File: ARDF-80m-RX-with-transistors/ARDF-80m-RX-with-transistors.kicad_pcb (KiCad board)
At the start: 2 copper layers, 44.5 x 26 mm, 45 parts, among them J1 JACK, Q1 BC847, Q2 BC847, Q3 BC847, Q4 BC847, Q5 BC847, U1 LM358, Y1 3.5795MHz

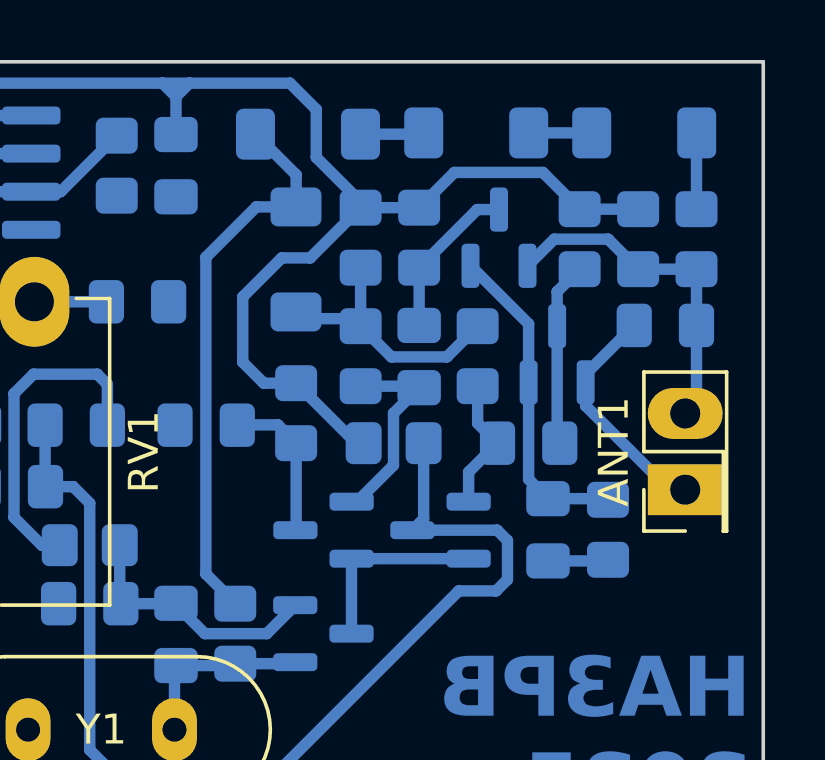
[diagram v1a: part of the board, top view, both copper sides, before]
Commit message: Update diodes packaging
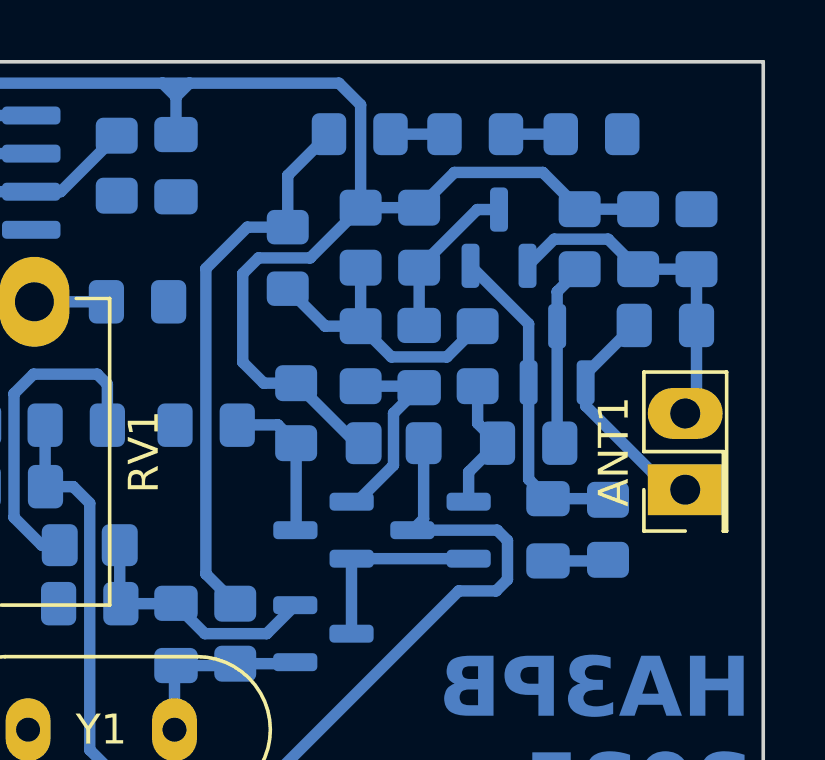
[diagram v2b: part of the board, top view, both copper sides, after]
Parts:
- D1, D2, D3, D5: footprint Diode_SMD:D_MiniMELF -> Diode_SMD:D_0805_2012Metric_Pad1.15x1.40mm_HandSolder
- moved D5 1.76 mm to (89.2, 79.8)
- moved D2 1.72 mm to (81.5, 79.8)
- moved D1 0.28 mm to (79.1, 84.0)
- moved D3 0.05 mm to (85.3, 79.8)
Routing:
- net GND: track 15.5 -> 12.9 mm
- net VCC: track 86.8 -> 88.2 mm
- net /BIAS: track 9.05 -> 9.65 mm

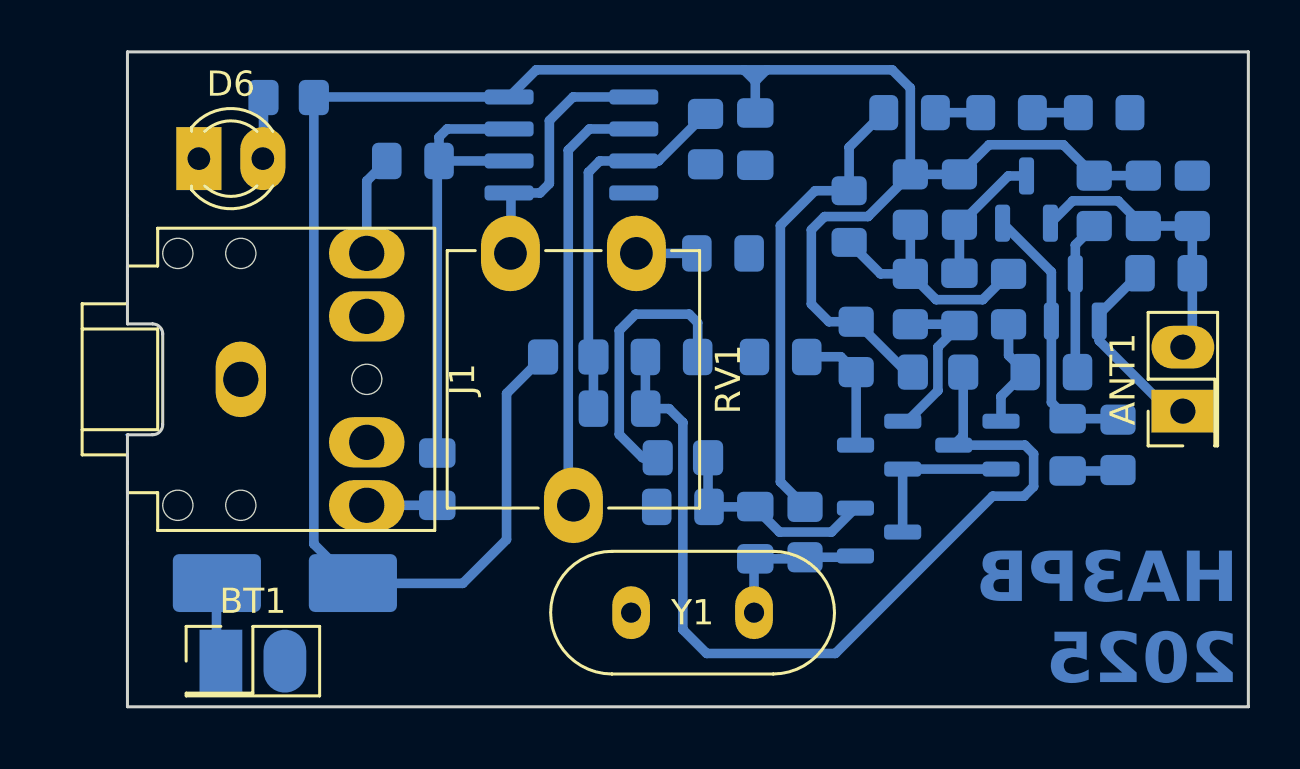
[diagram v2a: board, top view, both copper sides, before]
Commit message: Update jack connector footprint
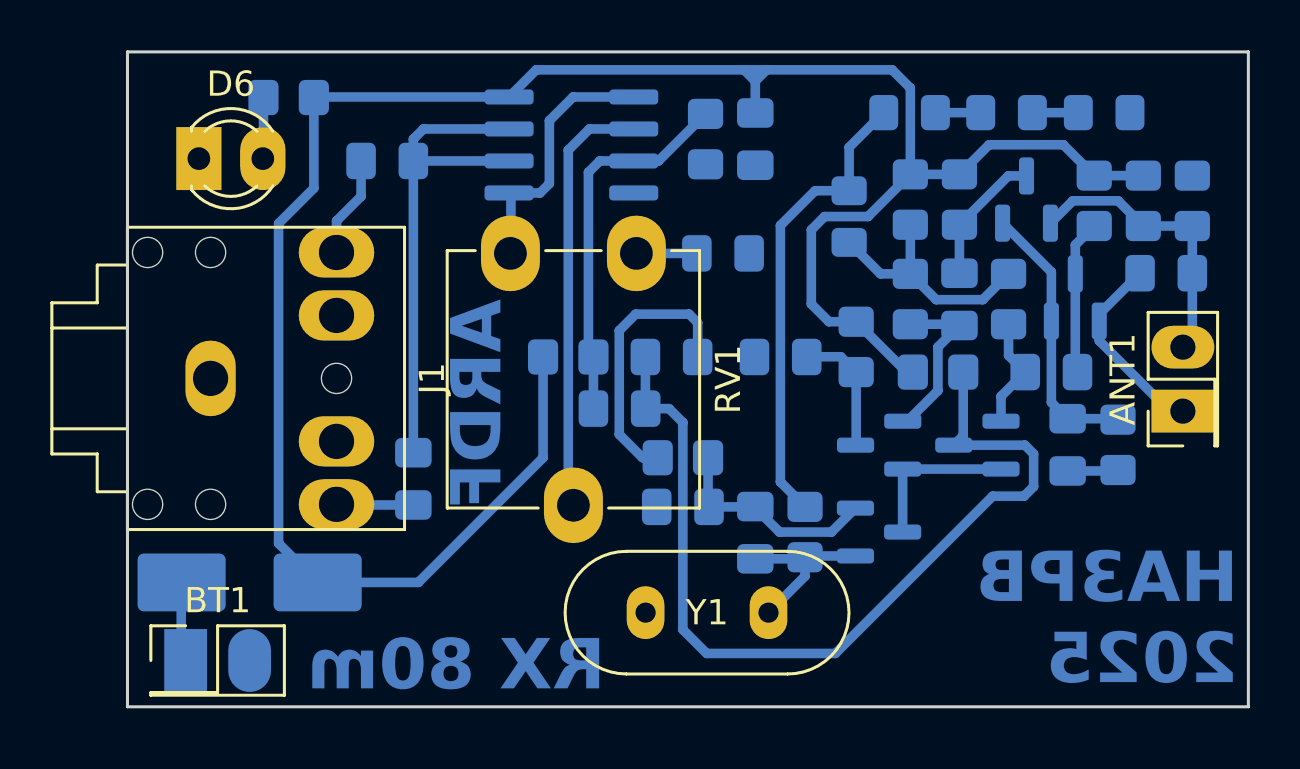
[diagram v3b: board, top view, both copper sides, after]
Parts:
- moved D4 1.40 mm to (55.3, 98.5)
- moved BT1 1.40 mm to (52.8, 101.6)
- moved J1 1.20 mm to (53.8, 90.4)
- moved C5 1.02 mm to (60.8, 81.8)
- moved C7 0.95 mm to (61.8, 94.4)
- moved Y1 0.58 mm to (71.0, 99.7)
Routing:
- net Net-(U1B--): track 18.3 -> 20.2 mm
- net VCC: track 88.2 -> 89.1 mm
- net Net-(Q5-B): track 6.21 -> 6.82 mm
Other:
- outline, holes or cut-outs redrawn
- board text added: "ARDF"
- board text added: "RX 80m"
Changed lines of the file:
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@@
 	(footprint "Crystal:Crystal_HC49-4H_Vertical"
 		(layer "F.Cu")
-		(at 70.445 99.7)
+		(at 71.02 99.7)
 		(descr "HC-49-4H, Crystal, http://5hertz.com/pdfs/04404_D.pdf")
 		(property "Reference" "Y1"
@@
 	(footprint "Connector_Audio:Jack_3.5mm_CUI_SJ1-3525N_Horizontal"
 		(layer "F.Cu")
-		(at 54.95 90.4375 -90)
+		(at 53.75 90.4 -90)
 		(descr "TRS 3.5mm, horizontal, through-hole, https://www.cuidevices.com/product/resource/pdf/sj1-352xn.pdf")
 		(tags "TRS audio jack stereo horizontal")
@@
 		)
 		(fp_line
-			(start -2.2 4.5)
-			(end -6.5 4.5)
-			(stroke
-				(width 0.12)
-				(type solid)
-			)
-			(layer "Edge.Cuts")
-		)
-		(fp_line
-			(start 2.2 4.5)
-			(end 6.5 4.5)
-			(stroke
-				(width 0.12)
-				(type solid)
-			)
-			(layer "Edge.Cuts")
-		)
-		(fp_line
-			(start -2.2 3.5)
-			(end -2.2 4.5)
-			(stroke
-				(width 0.12)
-				(type solid)
-			)
-			(layer "Edge.Cuts")
-		)
-		(fp_line
-			(start 2.2 3.5)
-			(end 2.2 4.5)
-			(stroke
-				(width 0.12)
-				(type solid)
-			)
-			(layer "Edge.Cuts")
-		)
-		(fp_line
-			(start 1.8 3.1)
-			(end -1.8 3.1)
-			(stroke
-				(width 0.12)
-				(type solid)
-			)
-			(layer "Edge.Cuts")
-		)
-		(fp_arc
-			(start -2.2 3.5)
-			(mid -2.082842 3.217158)
-			(end -1.8 3.1)
-			(stroke
-				(width 0.12)
-				(type solid)
-			)
-			(layer "Edge.Cuts")
-		)
-		(fp_arc
-			(start 1.8 3.1)
-			(mid 2.082843 3.217157)
-			(end 2.2 3.5)
+			(start 6.6376 3.3)
+			(end -6.6376 3.3)
 			(stroke
 				(width 0.12)
@@
 	(footprint "Connector_PinHeader_2.54mm:PinHeader_2x01_P2.54mm_Vertical"
 		(layer "F.Cu")
-		(at 54.16 101.625)
+		(at 52.76 101.6)
 		(descr "Through hole straight pin header, 2x01, 2.54mm pitch, double rows")
 		(tags "Through hole pin header THT 2x01 2.54mm double row")
@@
 	(footprint "Diode_SMD:D_SMB_Handsoldering"
 		(layer "B.Cu")
-		(at 56.7 98.525 180)
+		(at 55.3 98.5 180)
 		(descr "Diode SMB (DO-214AA) Handsoldering")
 		(tags "Diode SMB (DO-214AA) Handsoldering")
@@
 	(footprint "Capacitor_SMD:C_0805_2012Metric_Pad1.18x1.45mm_HandSolder"
 		(layer "B.Cu")
-		(at 62.75 94.4 90)
+		(at 61.8 94.3875 90)
 		(descr "Capacitor SMD 0805 (2012 Metric), square (rectangular) end terminal, IPC-7351 nominal with elongated pad for handsoldering. (Body size source: IPC-SM-782 page 76, https://www.pcb-3d.com/wordpress/wp-content/uploads/ipc-sm-782a_amendment_1_and_2.pdf, https://docs.google.com/spreadsheets/d/1BsfQQcO9C6DZCsRaXUlFlo91Tg2WpOkGARC1WS5S8t0/edit?usp=sharing), generated with kicad-footprint-generator")
 		(tags "capacitor handsolder")
@@
 	(footprint "Capacitor_SMD:C_0805_2012Metric_Pad1.18x1.45mm_HandSolder"
 		(layer "B.Cu")
-		(at 61.7825 81.7675 180)
+		(at 60.7625 81.7675 180)
 		(descr "Capacitor SMD 0805 (2012 Metric), square (rectangular) end terminal, IPC-7351 nominal with elongated pad for handsoldering. (Body size source: IPC-SM-782 page 76, https://www.pcb-3d.com/wordpress/wp-content/uploads/ipc-sm-782a_amendment_1_and_2.pdf, https://docs.google.com/spreadsheets/d/1BsfQQcO9C6DZCsRaXUlFlo91Tg2WpOkGARC1WS5S8t0/edit?usp=sharing), generated with kicad-footprint-generator")
 		(tags "capacitor handsolder")
@@
 	)
 	(gr_line
-		(start 50.45 96.9375)
+		(start 50.45 97.0376)
 		(end 50.45 103.4375)
 		(stroke
@@
 	)
 	(gr_line
-		(start 50.45 83.9375)
+		(start 50.45 83.7624)
 		(end 50.45 77.4375)
 		(stroke
@@
 		)
 	)
+	(gr_text "RX 80m"
+		(at 63.5 102.95 0)
+		(layer "B.Cu" knockout)
+		(effects
+			(font
+				(size 2 2)
+				(thickness 0.5)
+				(bold yes)
+			)
+			(justify bottom mirror)
+		)
+	)
+	(gr_text "ARDF"
+		(at 65.5 87.25 90)
+		(layer "B.Cu")
+		(effects
+			(font
+				(size 2 2)
+				(thickness 0.5)
+				(bold yes)
+			)
+			(justify left bottom mirror)
+		)
+	)
 	(segment
 		(start 89.03 88.905)
@@
 	)
 	(segment
-		(start 54.16 101.625)
-		(end 53.985 101.45)
+		(start 52.76 101.6)
+		(end 52.585 101.425)
 		(width 0.381)
 		(layer "B.Cu")
@@
 	)
 	(segment
-		(start 53.985 101.45)
-		(end 53.985 98.6975)
+		(start 52.585 101.425)
+		(end 52.585 98.6725)
 		(width 0.381)
 		(layer "B.Cu")
@@
 	)
 	(segment
-		(start 53.985 98.6975)
-		(end 53.825 98.5375)
+		(start 52.585 98.6725)
+		(end 52.425 98.5125)
 		(width 0.381)
 		(layer "B.Cu")
@@
 	)
 	(segment
-		(start 65.6 80.4975)
-		(end 63.14 80.4975)
+		(start 61.8 93.35)
+		(end 61.8 81.7675)
 		(width 0.381)
 		(layer "B.Cu")
@@
 	)
 	(segment
-		(start 62.82 80.8175)
-		(end 62.82 81.7675)
+		(start 65.6 81.7675)
+		(end 61.8 81.7675)
 		(width 0.381)
 		(layer "B.Cu")
@@
 	)
 	(segment
-		(start 62.82 81.7675)
-		(end 62.82 82.0675)
+		(start 62.2025 80.4975)
+		(end 61.8 80.9)
 		(width 0.381)
 		(layer "B.Cu")
@@
 	)
 	(segment
-		(start 62.75 82.1375)
-		(end 62.75 93.3625)
+		(start 61.8 80.9)
+		(end 61.8 81.7675)
 		(width 0.381)
 		(layer "B.Cu")
@@
 	)
 	(segment
-		(start 65.6 81.7675)
-		(end 62.82 81.7675)
+		(start 65.6 80.4975)
+		(end 62.2025 80.4975)
 		(width 0.381)
 		(layer "B.Cu")
@@
 	)
 	(segment
-		(start 62.82 82.0675)
-		(end 62.75 82.1375)
+		(start 58.75 85.4)
+		(end 58.75 84.15)
 		(width 0.381)
 		(layer "B.Cu")
-		(net 12)
+		(net 13)
 	)
 	(segment
-		(start 63.14 80.4975)
-		(end 62.82 80.8175)
+		(start 59.725 83.175)
+		(end 59.725 81.7675)
 		(width 0.381)
 		(layer "B.Cu")
-		(net 12)
+		(net 13)
 	)
 	(segment
-		(start 59.95 85.4375)
-		(end 59.95 82.5625)
+		(start 58.75 84.15)
+		(end 59.725 83.175)
 		(width 0.381)
 		(layer "B.Cu")
@@
 	)
 	(segment
-		(start 59.95 82.5625)
-		(end 60.745 81.7675)
+		(start 58.775 95.425)
+		(end 58.75 95.4)
 		(width 0.381)
 		(layer "B.Cu")
-		(net 13)
+		(net 14)
 	)
 	(segment
-		(start 62.75 95.4375)
-		(end 59.95 95.4375)
+		(start 61.8 95.425)
+		(end 58.775 95.425)
 		(width 0.381)
 		(layer "B.Cu")
@@
 	)
 	(segment
-		(start 79.3 97.5)
-		(end 79.35 97.45)
+		(start 77.35 98.25)
+		(end 75.9 99.7)
 		(width 0.381)
 		(layer "B.Cu")
@@
 	)
 	(segment
-		(start 75.325 99.7)
-		(end 75.325 97.5625)
+		(start 79.35 97.45)
+		(end 77.4 97.45)
 		(width 0.381)
 		(layer "B.Cu")
@@
 	)
 	(segment
-		(start 75.325 97.5625)
-		(end 77.2375 97.5625)
+		(start 77.2875 97.5625)
+		(end 77.35 97.5)
 		(width 0.381)
 		(layer "B.Cu")
@@
 	)
 	(segment
-		(start 77.3 97.5)
-		(end 79.3 97.5)
+		(start 75.375 97.5625)
+		(end 77.2875 97.5625)
 		(width 0.381)
 		(layer "B.Cu")
@@
 	)
 	(segment
-		(start 77.2375 97.5625)
-		(end 77.3 97.5)
+		(start 77.4 97.45)
+		(end 77.35 97.5)
+		(width 0.381)
+		(layer "B.Cu")
+		(net 17)
+	)
+	(segment
+		(start 77.35 97.5)
+		(end 77.35 98.25)
 		(width 0.381)
 		(layer "B.Cu")
@@
 	)
 	(segment
-		(start 57.85 96.975)
-		(end 59.4125 98.5375)
-		(width 0.381)
-		(layer "B.Cu")
-		(net 23)
-	)
-	(segment
-		(start 59.4125 98.5375)
-		(end 63.7625 98.5375)
-		(width 0.381)
-		(layer "B.Cu")
-		(net 23)
-	)
-	(segment
 		(start 81.63 90.15)
 		(end 81.38 90.15)
@@
 	)
 	(segment
-		(start 65.5 96.8)
-		(end 65.5 91)
+		(start 66.95 93.55)
+		(end 62 98.5)
 		(width 0.381)
 		(layer "B.Cu")
@@
 	)
 	(segment
+		(start 57.85 82.85)
+		(end 57.85 79.25)
+		(width 0.381)
+		(layer "B.Cu")
+		(net 23)
+	)
+	(segment
 		(start 83.48 82.3)
 		(end 84.655 81.125)
@@
 	)
 	(segment
+		(start 62 98.5)
+		(end 58 98.5)
+		(width 0.381)
+		(layer "B.Cu")
+		(net 23)
+	)
+	(segment
 		(start 74.925 78.15)
 		(end 66.6775 78.15)
@@
 	)
 	(segment
-		(start 63.7625 98.5375)
-		(end 65.5 96.8)
-		(width 0.381)
-		(layer "B.Cu")
-		(net 23)
-	)
-	(segment
 		(start 75.825 78.15)
 		(end 80.807072 78.15)
@@
 	)
 	(segment
-		(start 65.5 91)
-		(end 66.95 89.55)
+		(start 87.605 81.125)
+		(end 88.83 82.35)
 		(width 0.381)
 		(layer "B.Cu")
@@
 	)
 	(segment
-		(start 87.605 81.125)
-		(end 88.83 82.35)
+		(start 66.95 89.55)
+		(end 66.95 93.55)
 		(width 0.381)
 		(layer "B.Cu")
@@
 	)
 	(segment
+		(start 58 98.5)
+		(end 56.45 96.95)
+		(width 0.381)
+		(layer "B.Cu")
+		(net 23)
+	)
+	(segment
 		(start 80.807072 78.15)
 		(end 81.53 78.872928)
@@
 	)
 	(segment
+		(start 56.45 96.95)
+		(end 56.45 84.25)
+		(width 0.381)
+		(layer "B.Cu")
+		(net 23)
+	)
+	(segment
 		(start 77.6 87.45)
 		(end 78.3 88.15)
@@
 	)
 	(segment
-		(start 57.85 79.25)
-		(end 57.85 96.975)
+		(start 56.45 84.25)
+		(end 57.85 82.85)
 		(width 0.381)
 		(layer "B.Cu")
@@
 		(polygon
 			(pts
-				(xy 50.45 77.4375) (xy 50.45 88.2375) (xy 51.45 88.2375) (xy 51.732843 88.354658) (xy 51.85 88.6375)
-				(xy 51.85 92.2375) (xy 51.732843 92.520343) (xy 51.45 92.6375) (xy 50.35 92.6375) (xy 50.45 92.6375)
-				(xy 50.45 103.4375) (xy 94.95 103.4375) (xy 94.95 77.4375)
+				(xy 50.45 77.4375) (xy 50.45 103.4375) (xy 94.95 103.4375) (xy 94.95 77.4375)
 			)
 		)
